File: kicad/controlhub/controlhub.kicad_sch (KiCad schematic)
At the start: 0 parts

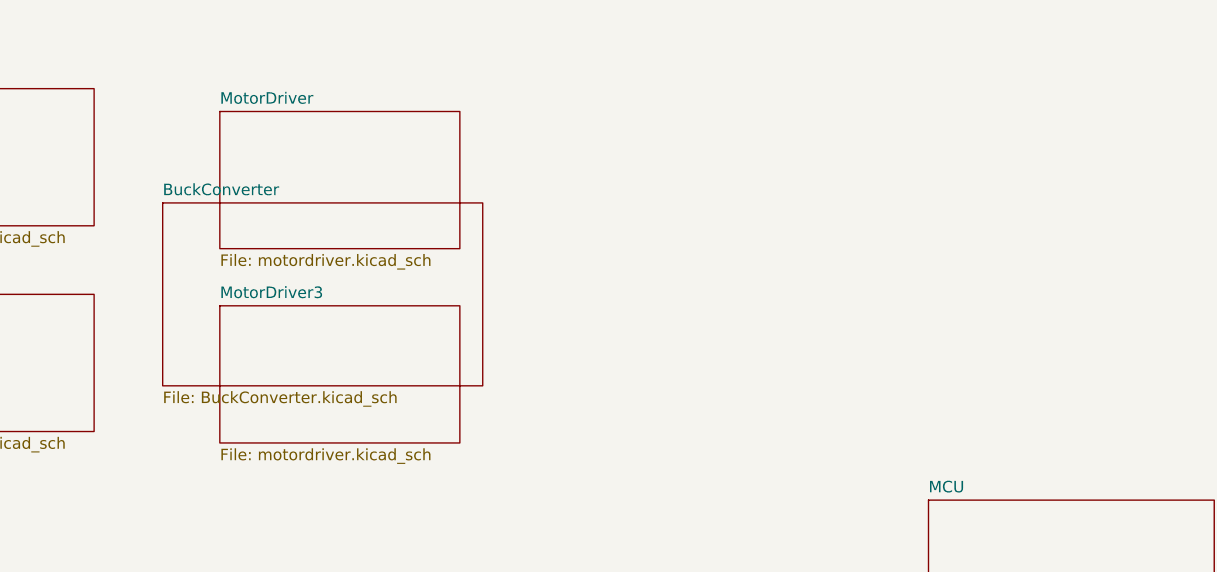
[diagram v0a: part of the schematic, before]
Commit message: fixed small overlap in diagrams
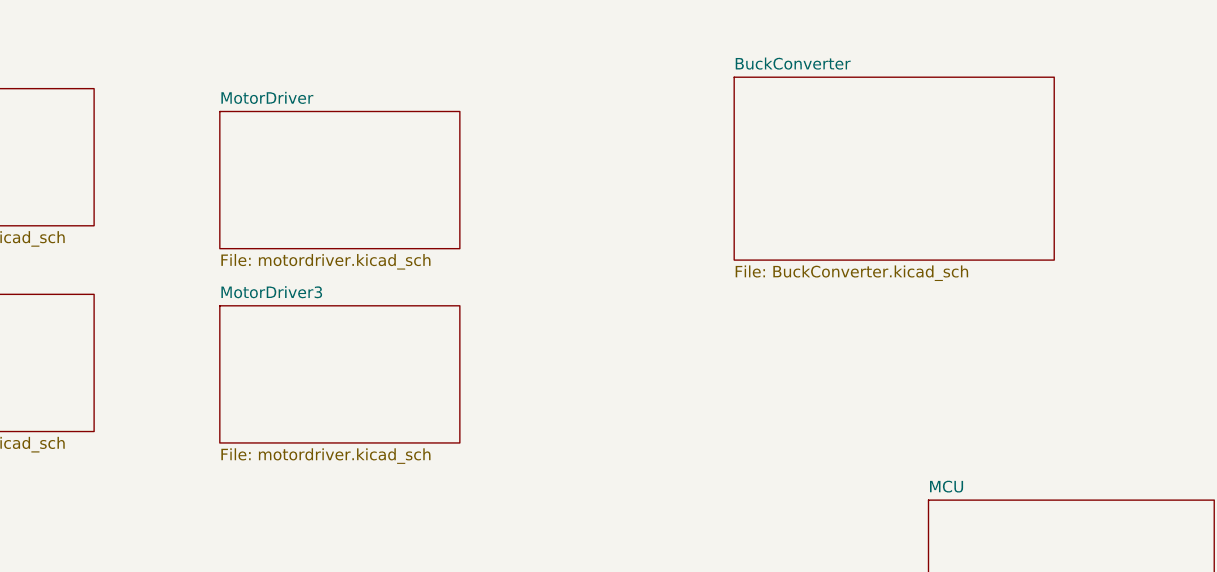
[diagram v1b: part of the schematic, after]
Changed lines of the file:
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@@
 	)
 	(sheet
-		(at 71.12 52.07)
+		(at 134.62 38.1)
 		(size 35.56 20.32)
 		(exclude_from_sim no)
@@
 		)
 		(property "Sheetname" "BuckConverter"
-			(at 71.12 51.3584 0)
+			(at 134.62 37.3884 0)
 			(effects
 				(font
@@
 		)
 		(property "Sheetfile" "BuckConverter.kicad_sch"
-			(at 71.12 72.9746 0)
+			(at 134.62 59.0046 0)
 			(effects
 				(font

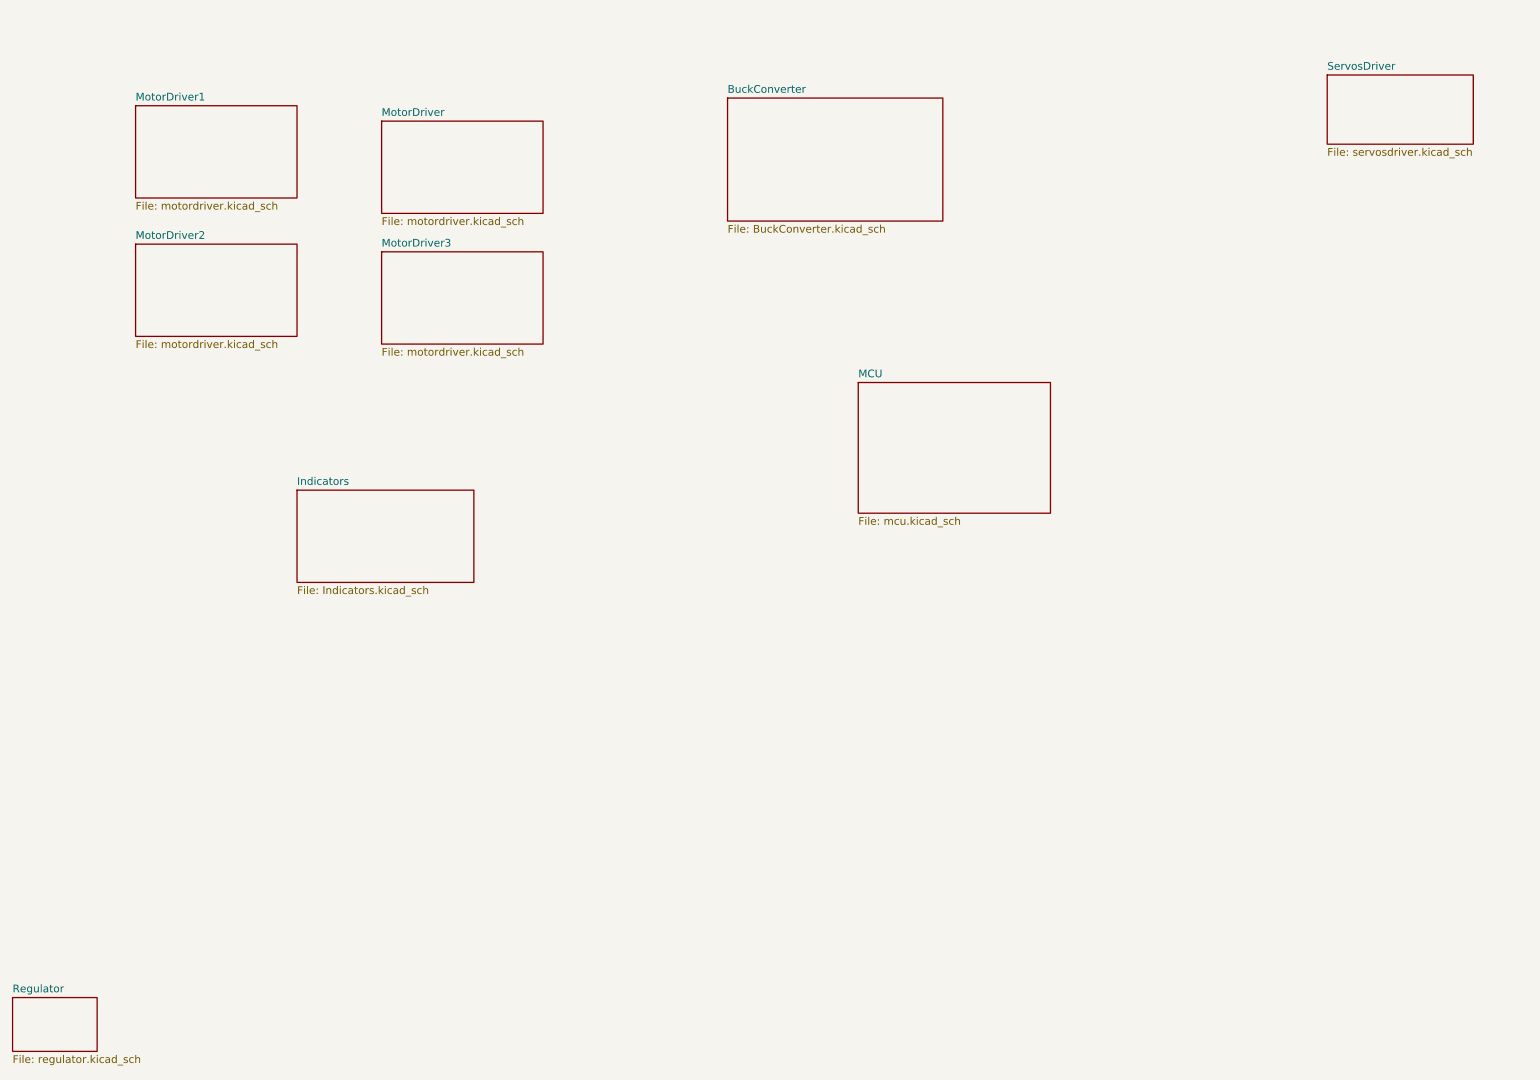
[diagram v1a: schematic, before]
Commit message: removed uneccesary schematics and worked on proper wiring
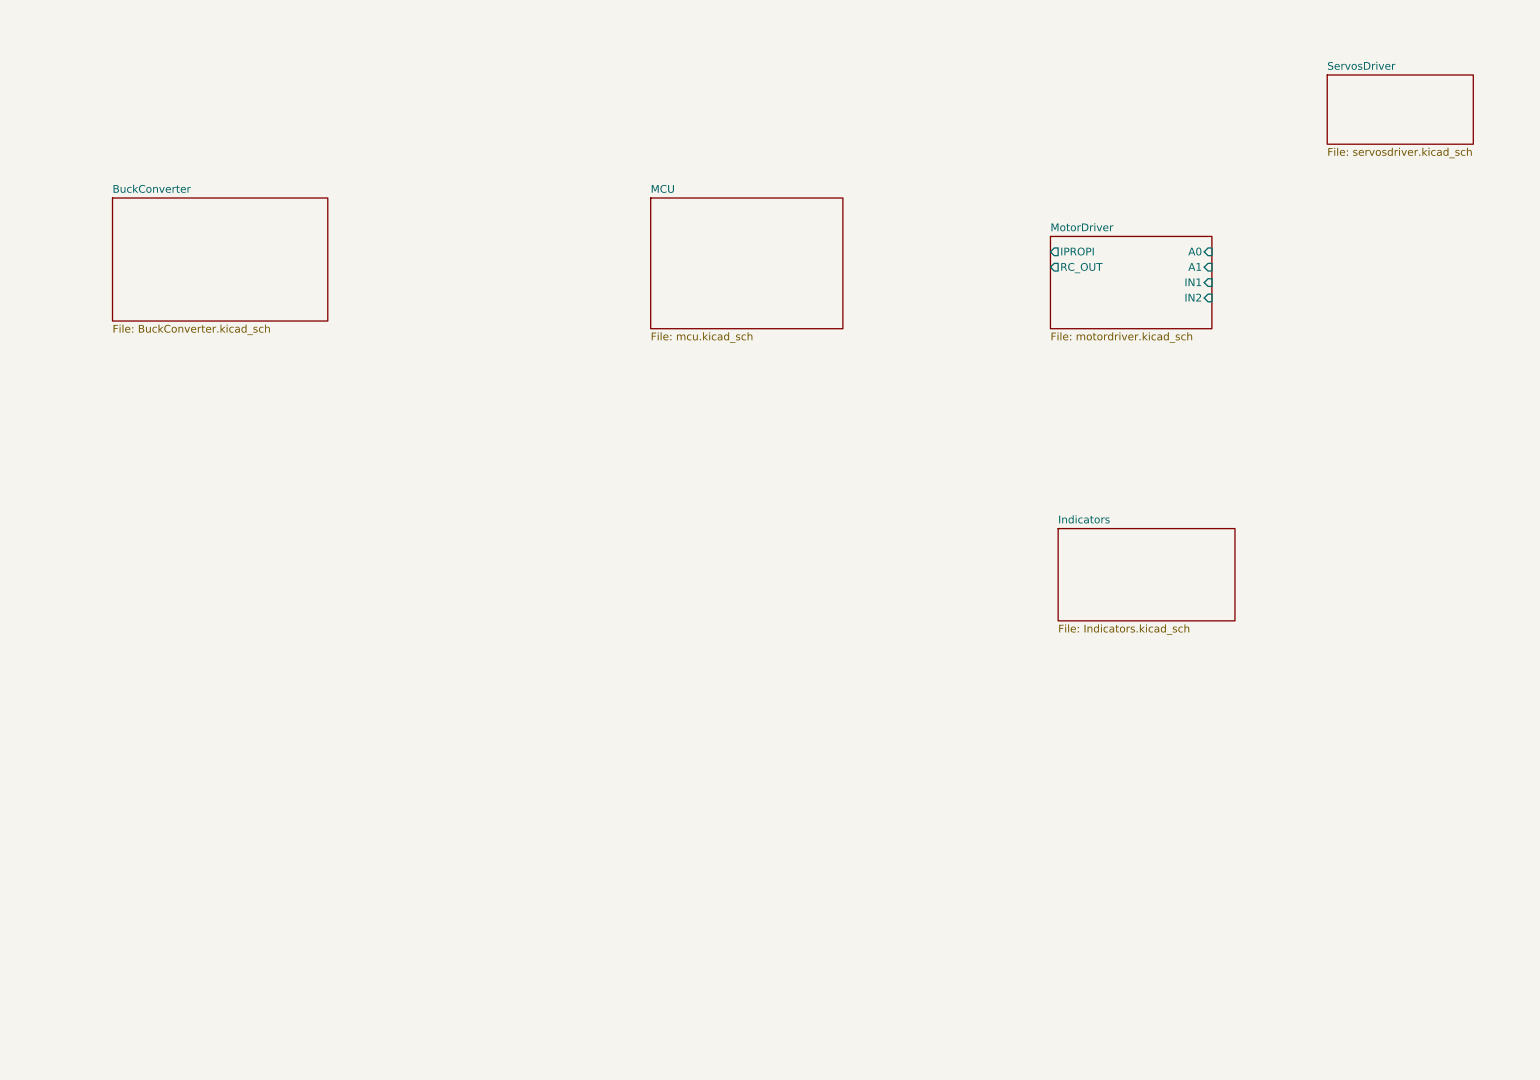
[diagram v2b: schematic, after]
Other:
- removed sheet MotorDriver1
- removed sheet MotorDriver2
- removed sheet MotorDriver3
- removed sheet Regulator
- sheet MotorDriver ports: added A0, A1, IN1, IN2, IPROPI, RC_OUT; removed none
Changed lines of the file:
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@@
 	)
 	(sheet
-		(at 63.5 102.87)
+		(at 189.23 109.22)
 		(size 29.21 15.24)
 		(exclude_from_sim no)
@@
 		)
 		(property "Sheetname" "Indicators"
-			(at 63.5 102.1584 0)
+			(at 189.23 108.5084 0)
 			(effects
 				(font
@@
 		)
 		(property "Sheetfile" "Indicators.kicad_sch"
-			(at 63.5 118.6946 0)
+			(at 189.23 125.0446 0)
 			(effects
 				(font
@@
 	)
 	(sheet
-		(at 134.62 38.1)
+		(at 33.02 54.61)
 		(size 35.56 20.32)
 		(exclude_from_sim no)
@@
 		)
 		(property "Sheetname" "BuckConverter"
-			(at 134.62 37.3884 0)
+			(at 33.02 53.8984 0)
 			(effects
 				(font
@@
 		)
 		(property "Sheetfile" "BuckConverter.kicad_sch"
-			(at 134.62 59.0046 0)
+			(at 33.02 75.5146 0)
 			(effects
 				(font
@@
 	)
 	(sheet
-		(at 77.47 41.91)
+		(at 187.96 60.96)
 		(size 26.67 15.24)
 		(exclude_from_sim no)
@@
 		)
 		(property "Sheetname" "MotorDriver"
-			(at 77.47 41.1984 0)
+			(at 187.96 60.2484 0)
 			(effects
 				(font
@@
 		)
 		(property "Sheetfile" "motordriver.kicad_sch"
-			(at 77.47 57.7346 0)
-			(effects
-				(font
-					(size 1.27 1.27)
-				)
-				(justify left top)
+			(at 187.96 76.7846 0)
+			(effects
+				(font
+					(size 1.27 1.27)
+				)
+				(justify left top)
+			)
+		)
+		(pin "A0" input
+			(at 214.63 63.5 0)
+			(effects
+				(font
+					(size 1.27 1.27)
+				)
+				(justify right)
+			)
+		)
+		(pin "A1" input
+			(at 214.63 66.04 0)
+			(effects
+				(font
+					(size 1.27 1.27)
+				)
+				(justify right)
+			)
+		)
+		(pin "IN1" input
+			(at 214.63 68.58 0)
+			(effects
+				(font
+					(size 1.27 1.27)
+				)
+				(justify right)
+			)
+		)
+		(pin "IN2" input
+			(at 214.63 71.12 0)
+			(effects
+				(font
+					(size 1.27 1.27)
+				)
+				(justify right)
+			)
+		)
+		(pin "IPROPI" output
+			(at 187.96 63.5 180)
+			(effects
+				(font
+					(size 1.27 1.27)
+				)
+				(justify left)
+			)
+		)
+		(pin "RC_OUT" output
+			(at 187.96 66.04 180)
+			(effects
+				(font
+					(size 1.27 1.27)
+				)
+				(justify left)
 			)
 		)
@@
 	)
 	(sheet
-		(at 156.21 85.09)
+		(at 121.92 54.61)
 		(size 31.75 21.59)
 		(exclude_from_sim no)
@@
 		)
 		(property "Sheetname" "MCU"
-			(at 156.21 84.3784 0)
+			(at 121.92 53.8984 0)
 			(effects
 				(font
@@
 		)
 		(property "Sheetfile" "mcu.kicad_sch"
-			(at 156.21 107.2646 0)
+			(at 121.92 76.7846 0)
 			(effects
 				(font
@@
 				(path "/78f9b8b9-94ed-46bb-ab2b-797c156bf665"
 					(page "4")
-				)
-			)
-		)
-	)
-	(sheet
-		(at 36.83 62.23)
-		(size 26.67 15.24)
-		(exclude_from_sim no)
-		(in_bom yes)
-		(on_board yes)
-		(dnp no)
-		(fields_autoplaced yes)
-		(stroke
-			(width 0.1524)
-			(type solid)
-		)
-		(fill
-			(color 0 0 0 0.0000)
-		)
-		(property "Sheetname" "MotorDriver2"
-			(at 36.83 61.5184 0)
-			(effects
-				(font
-					(size 1.27 1.27)
-				)
-				(justify left bottom)
-			)
-		)
-		(property "Sheetfile" "motordriver.kicad_sch"
-			(at 36.83 78.0546 0)
-			(effects
-				(font
-					(size 1.27 1.27)
-				)
-				(justify left top)
-			)
-		)
-		(instances
-			(project "controlhub"
-				(path "/78f9b8b9-94ed-46bb-ab2b-797c156bf665"
-					(page "8")
-				)
-			)
-		)
-	)
-	(sheet
-		(at 16.51 186.69)
-		(size 13.97 8.89)
-		(exclude_from_sim no)
-		(in_bom yes)
-		(on_board yes)
-		(dnp no)
-		(fields_autoplaced yes)
-		(stroke
-			(width 0.1524)
-			(type solid)
-		)
-		(fill
-			(color 0 0 0 0.0000)
-		)
-		(property "Sheetname" "Regulator"
-			(at 16.51 185.9784 0)
-			(effects
-				(font
-					(size 1.27 1.27)
-				)
-				(justify left bottom)
-			)
-		)
-		(property "Sheetfile" "regulator.kicad_sch"
-			(at 16.51 196.1646 0)
-			(effects
-				(font
-					(size 1.27 1.27)
-				)
-				(justify left top)
-			)
-		)
-		(instances
-			(project "controlhub"
-				(path "/78f9b8b9-94ed-46bb-ab2b-797c156bf665"
-					(page "2")
-				)
-			)
-		)
-	)
-	(sheet
-		(at 36.83 39.37)
-		(size 26.67 15.24)
-		(exclude_from_sim no)
-		(in_bom yes)
-		(on_board yes)
-		(dnp no)
-		(fields_autoplaced yes)
-		(stroke
-			(width 0.1524)
-			(type solid)
-		)
-		(fill
-			(color 0 0 0 0.0000)
-		)
-		(property "Sheetname" "MotorDriver1"
-			(at 36.83 38.6584 0)
-			(effects
-				(font
-					(size 1.27 1.27)
-				)
-				(justify left bottom)
-			)
-		)
-		(property "Sheetfile" "motordriver.kicad_sch"
-			(at 36.83 55.1946 0)
-			(effects
-				(font
-					(size 1.27 1.27)
-				)
-				(justify left top)
-			)
-		)
-		(instances
-			(project "controlhub"
-				(path "/78f9b8b9-94ed-46bb-ab2b-797c156bf665"
-					(page "7")
 				)
 			)
@@
 				)
 			)
-		)
-	)
-	(sheet
-		(at 77.47 63.5)
-		(size 26.67 15.24)
-		(exclude_from_sim no)
-		(in_bom yes)
-		(on_board yes)
-		(dnp no)
-		(fields_autoplaced yes)
-		(stroke
-			(width 0.1524)
-			(type solid)
-		)
-		(fill
-			(color 0 0 0 0.0000)
-		)
-		(property "Sheetname" "MotorDriver3"
-			(at 77.47 62.7884 0)
-			(effects
-				(font
-					(size 1.27 1.27)
-				)
-				(justify left bottom)
-			)
-		)
-		(property "Sheetfile" "motordriver.kicad_sch"
-			(at 77.47 79.3246 0)
-			(effects
-				(font
-					(size 1.27 1.27)
-				)
-				(justify left top)
-			)
-		)
-		(instances
-			(project "controlhub"
-				(path "/78f9b8b9-94ed-46bb-ab2b-797c156bf665"
-					(page "9")
-				)
-			)

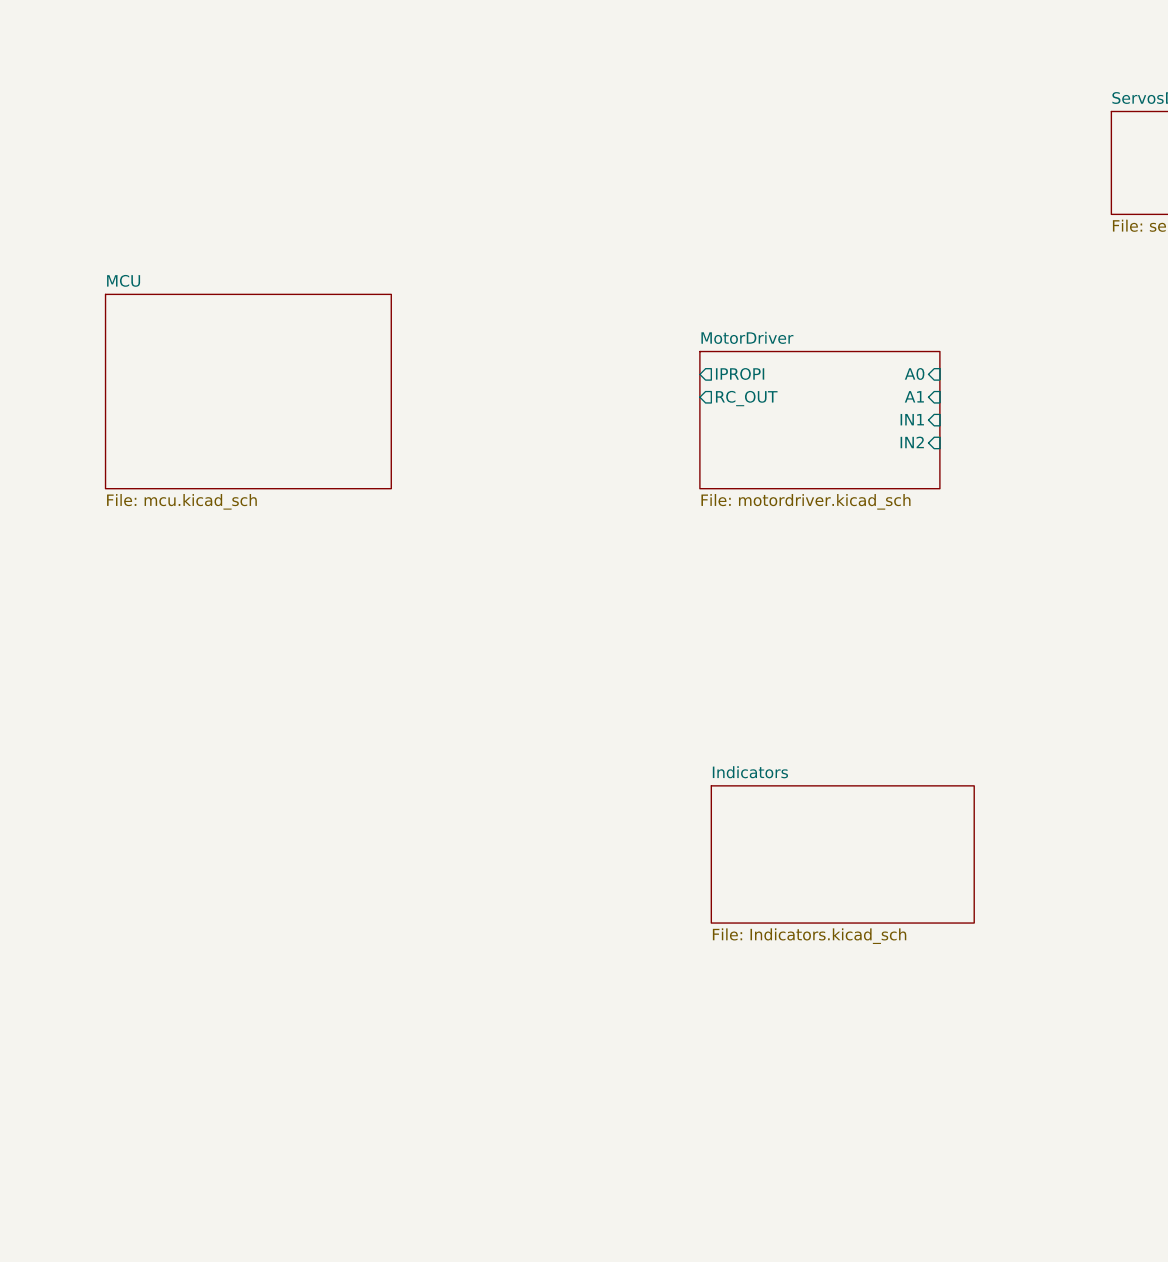
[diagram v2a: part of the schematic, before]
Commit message: added filters and kept working on wiring schematics
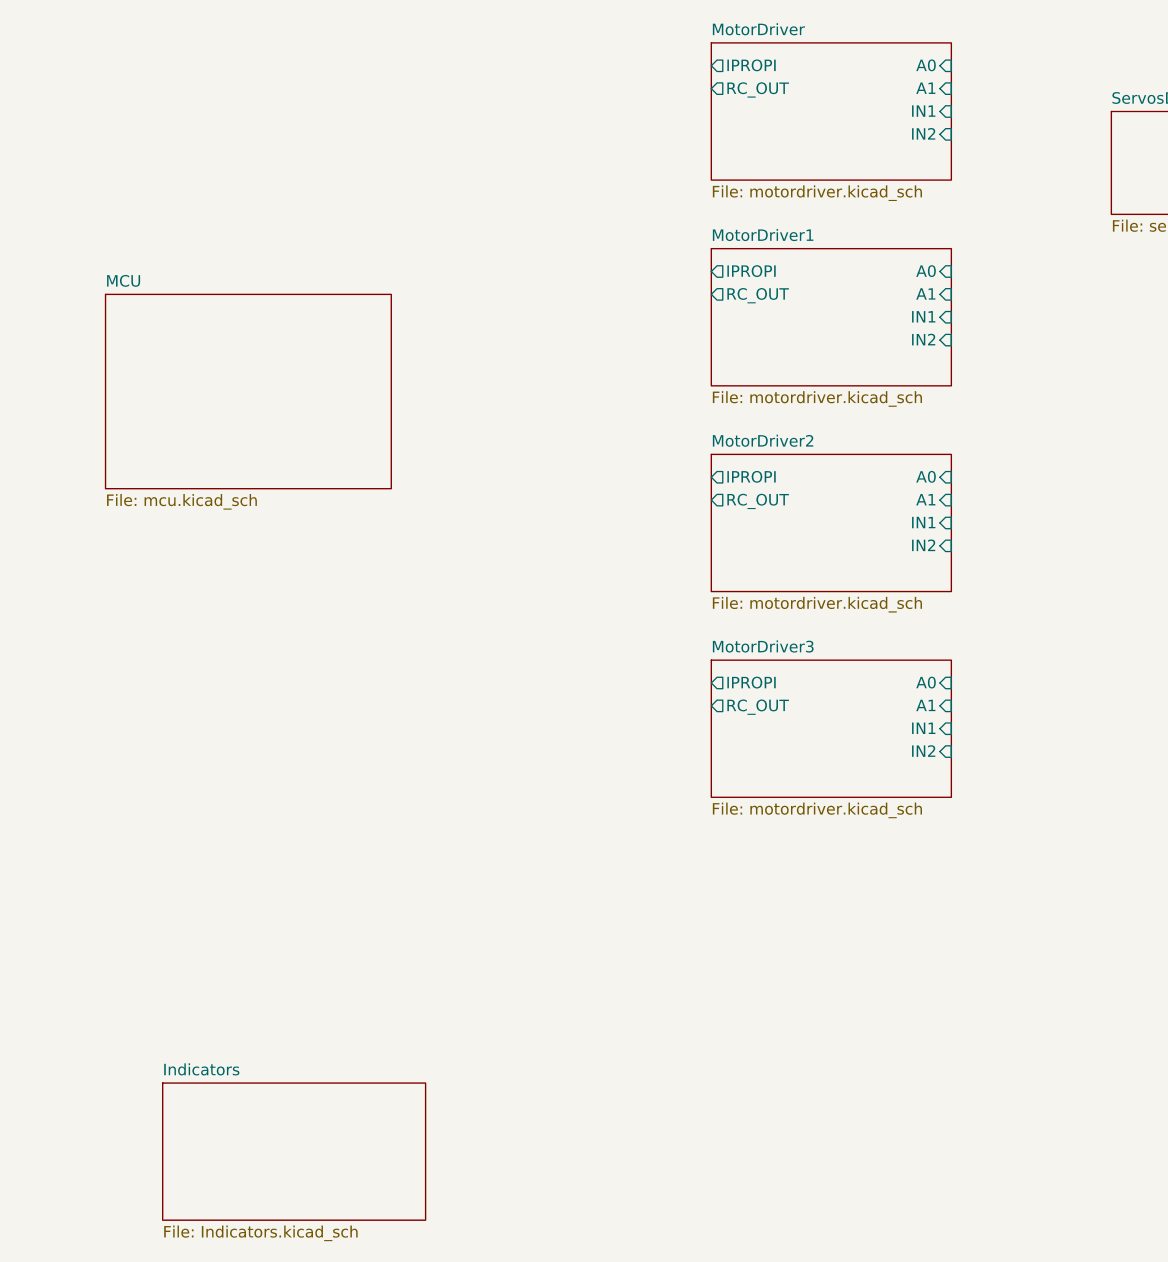
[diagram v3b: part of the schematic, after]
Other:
- added sheet MotorDriver1 (motordriver.kicad_sch)
- added sheet MotorDriver2 (motordriver.kicad_sch)
- added sheet MotorDriver3 (motordriver.kicad_sch)
